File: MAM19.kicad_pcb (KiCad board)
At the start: 2 copper layers, 224.2 x 179.1 mm, 101 parts, among them J06 PWM/IR C, J101 GNDC1, J102 GNDC2, J103 GNDD1, J104 GNDD2, J105 PWM/IR D, J107 HOLD1, J108 HOLD2, J181 +18C, J182 +18D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

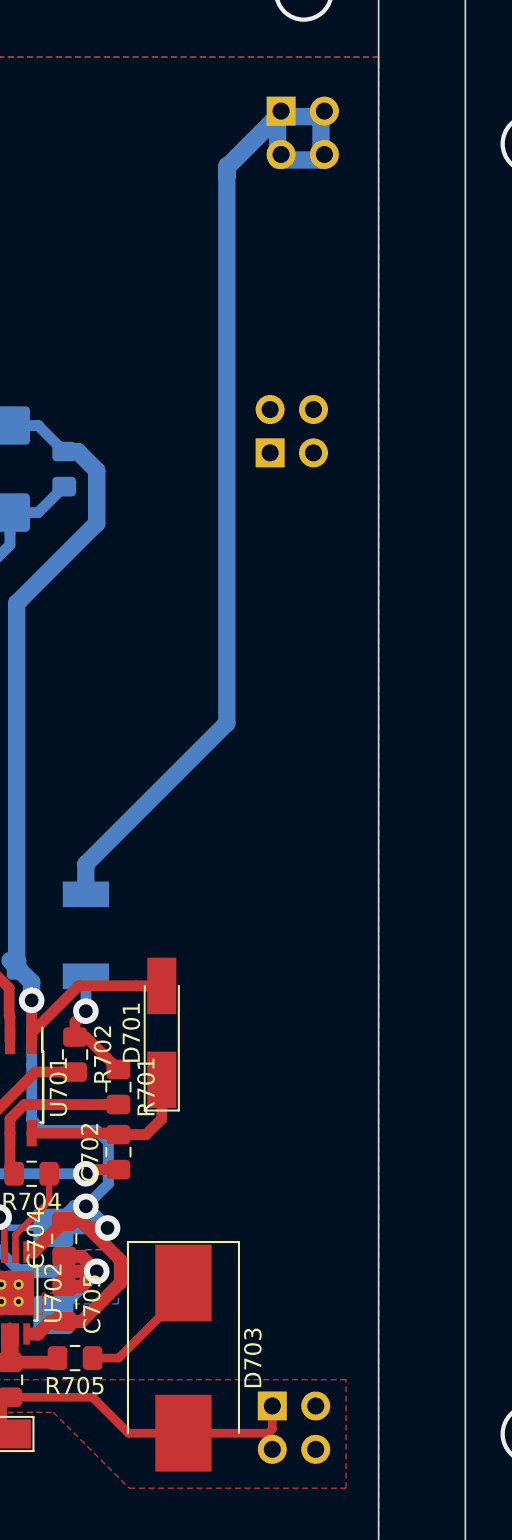
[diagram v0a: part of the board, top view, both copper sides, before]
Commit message: connectors moved
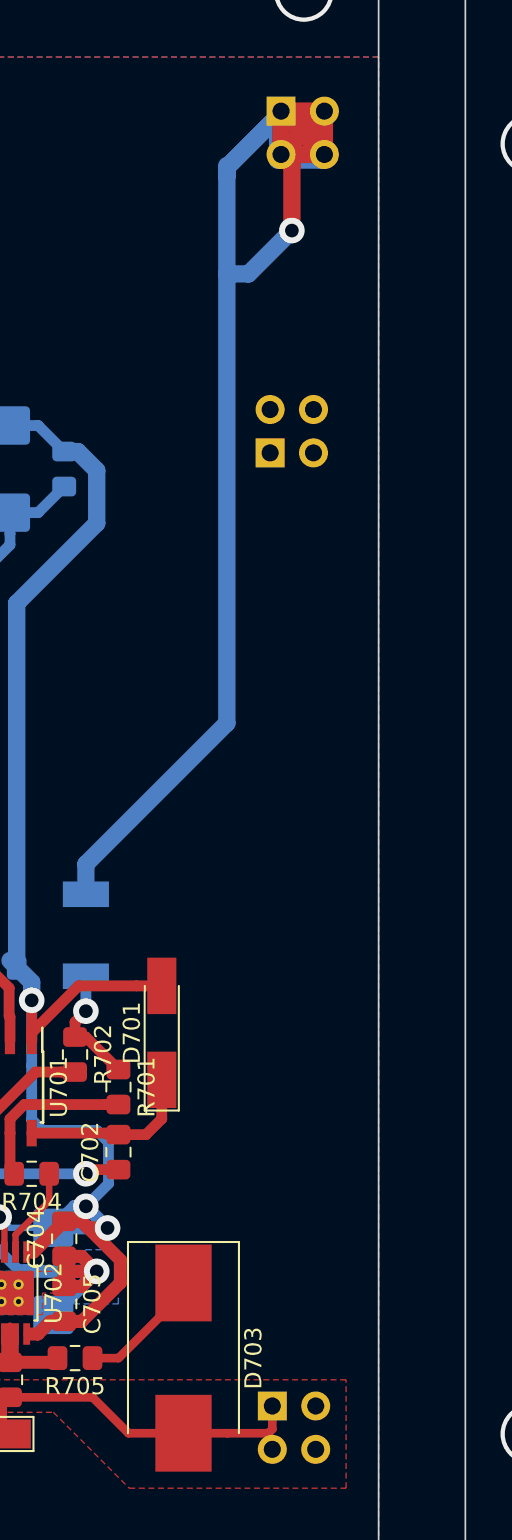
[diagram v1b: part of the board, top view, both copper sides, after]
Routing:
- net /chopper/-MOTOR: track 66.2 -> 93.1 mm, vias 0 -> 1

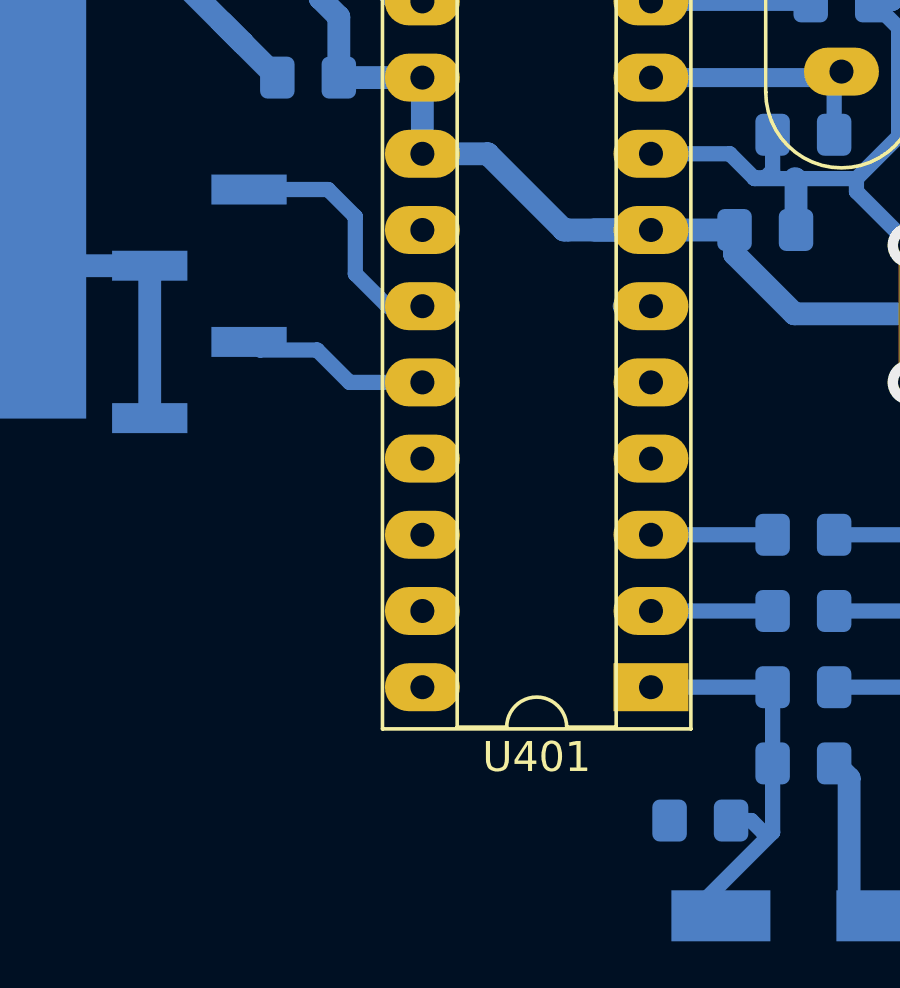
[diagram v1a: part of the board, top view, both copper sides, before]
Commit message: pinos pwm e fault alterados de acordo com o sugerido em #1
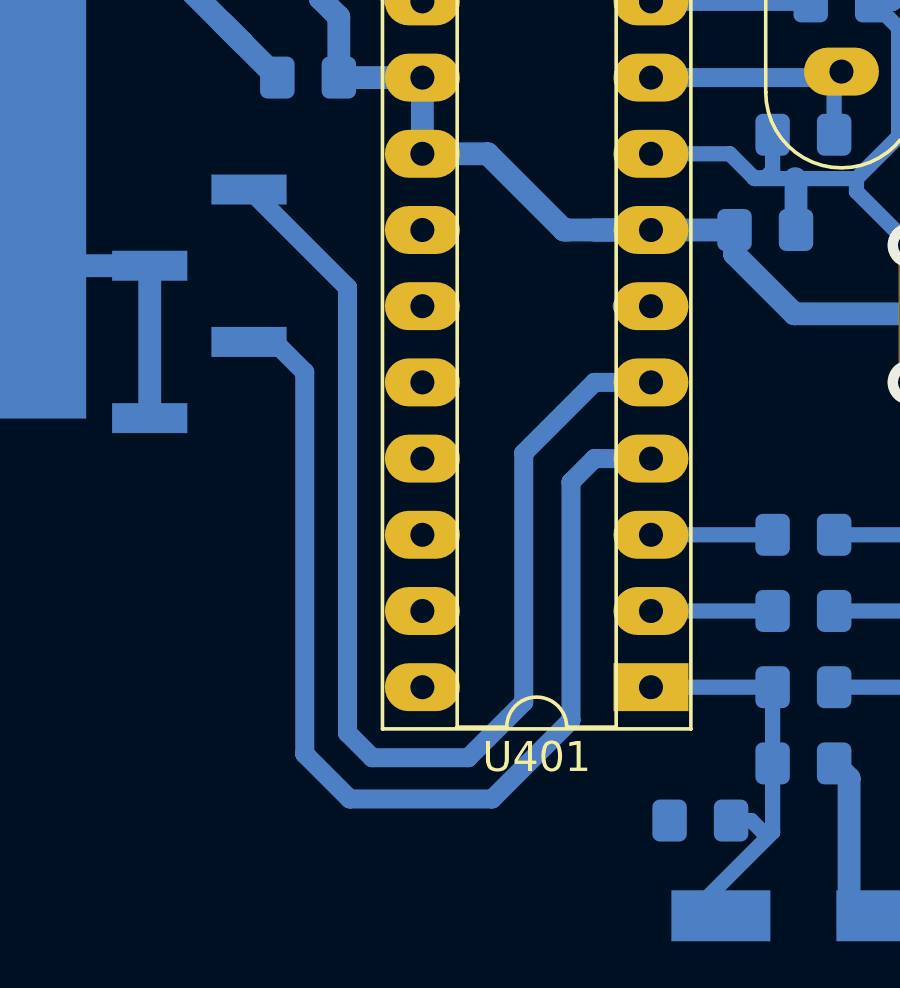
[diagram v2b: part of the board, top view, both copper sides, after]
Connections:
- U201 pad 5: Net-(U201-Pad5) -> (no net)
- U202 pad 10: Net-(U202-Pad10) -> (no net)
- U202 pad 11: Net-(U202-Pad11) -> (no net)
- U202 pad 3: Net-(U202-Pad3) -> (no net)
- U202 pad 4: Net-(U202-Pad4) -> (no net)
- U202 pad 5: Net-(U202-Pad5) -> (no net)
- U202 pad 6: Net-(U202-Pad6) -> (no net)
- U401 pad 11: Net-(U401-Pad11) -> (no net)
- U401 pad 12: Net-(U401-Pad12) -> (no net)
- U401 pad 16: Net-(U401-Pad16) -> (no net)
- U401 pad 23: /MCU/PWM -> (no net)
- U401 pad 24: /MCU/IR_2127_FAULT -> (no net)
- U401 pad 25: Net-(U401-Pad25) -> (no net)
- U401 pad 26: Net-(U401-Pad26) -> (no net)
- U401 pad 27: Net-(U401-Pad27) -> (no net)
- U401 pad 28: Net-(U401-Pad28) -> (no net)
- U401 pad 4: Net-(U401-Pad4) -> /MCU/IR_2127_FAULT
- U401 pad 5: Net-(U401-Pad5) -> /MCU/PWM
- U401 pad 6: Net-(U401-Pad6) -> (no net)
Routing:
- net /MCU/PWM: track 8.78 -> 40.4 mm
- net /MCU/IR_2127_FAULT: track 6.97 -> 36.5 mm
- net (no net): track 0.00 -> 2.38 mm
- net Net-(U401-Pad6): track 1.41 -> 0.00 mm
